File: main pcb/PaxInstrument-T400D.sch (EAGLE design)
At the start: 88 parts, among them IC2 NC7S00DBV, J1 MICRO-SDCARD-CONNECTOR-330006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, Q1 DMP2035U-7, U2 APX809, U3 MCP73831, U4 MIC5219-3.3V, X1 FH12-12S-1S, X2 FH12-12S-0.5SH, Y1 RESONATORSMD

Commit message: - Not sure what changed. This is still just playing around.
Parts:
- removed ICSP, ICSP1: ICSP, PaxInstrument-T400:SPARKFUN-CONNECTORS_M03X2PAX
- added JP13, JP14, JP15, JP16, JP17: M01PTH, SparkFun-Connectors:M01PTH
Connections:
- net 3.3V: no longer ICSP1.6
- net DATA1: no longer ICSP1.3
- net DATA2: no longer ICSP1.4
- net GND: no longer ICSP.6, ICSP1.5
- net MISO: now also JP13.1; no longer ICSP.1
- net MOSI: now also JP17.1; no longer ICSP.4
- net RESET: now also JP15.1; no longer ICSP.5
- net SCK: now also JP14.1; no longer ICSP.3
- net SCL: no longer ICSP1.1
- net SDA: no longer ICSP1.2
- net VBUS_IN: now also JP16.1; no longer ICSP.2
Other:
- note removed: "ICSP"
- note removed: "Programming"

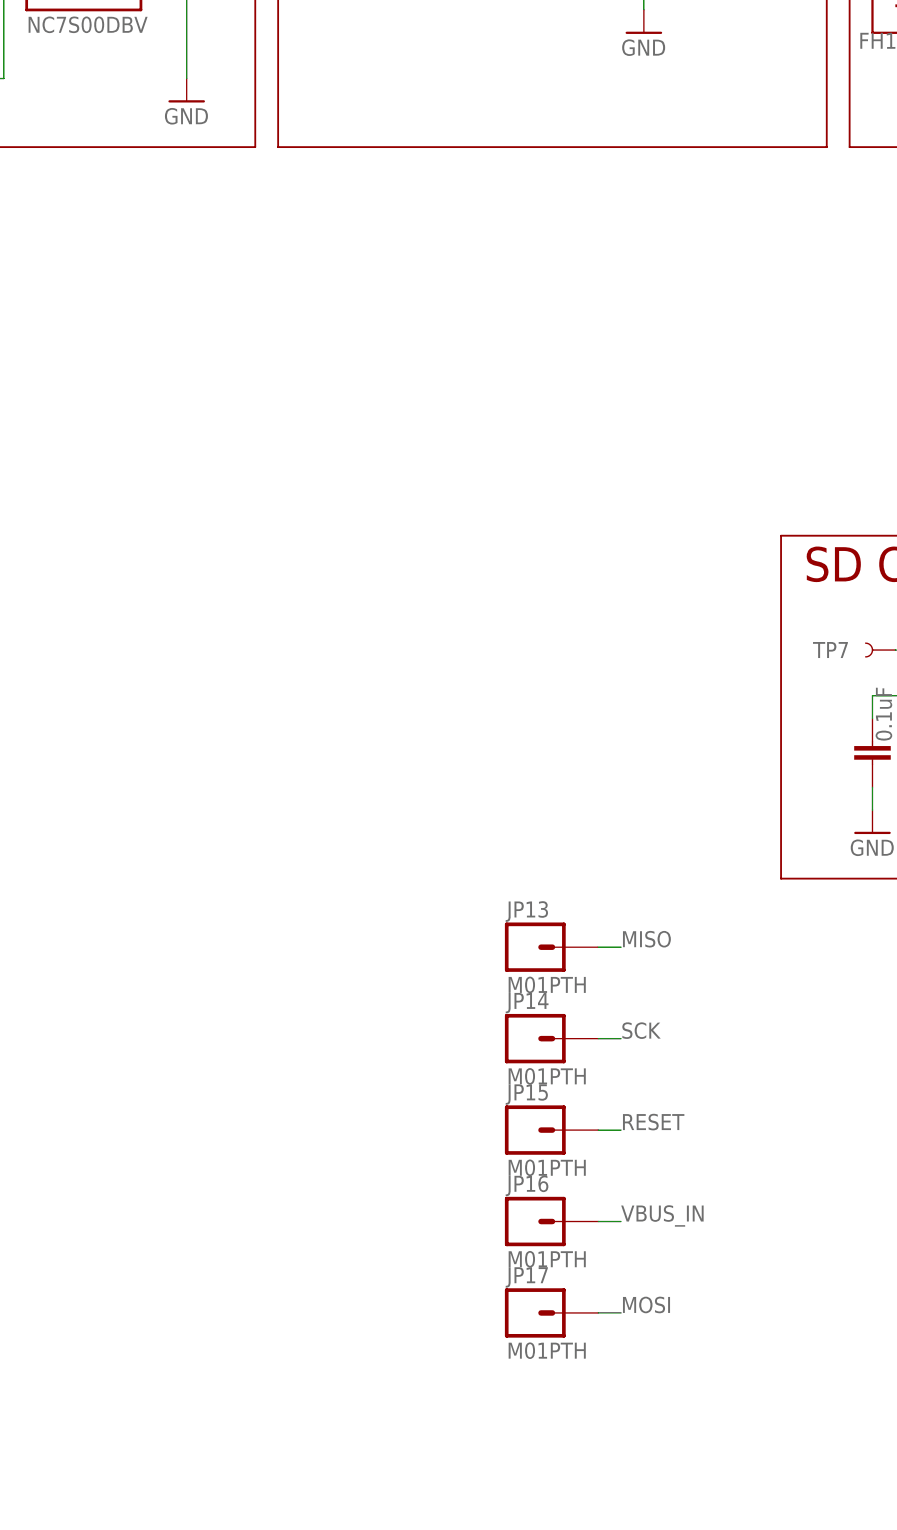
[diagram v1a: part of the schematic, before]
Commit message: Lengthened the modules.
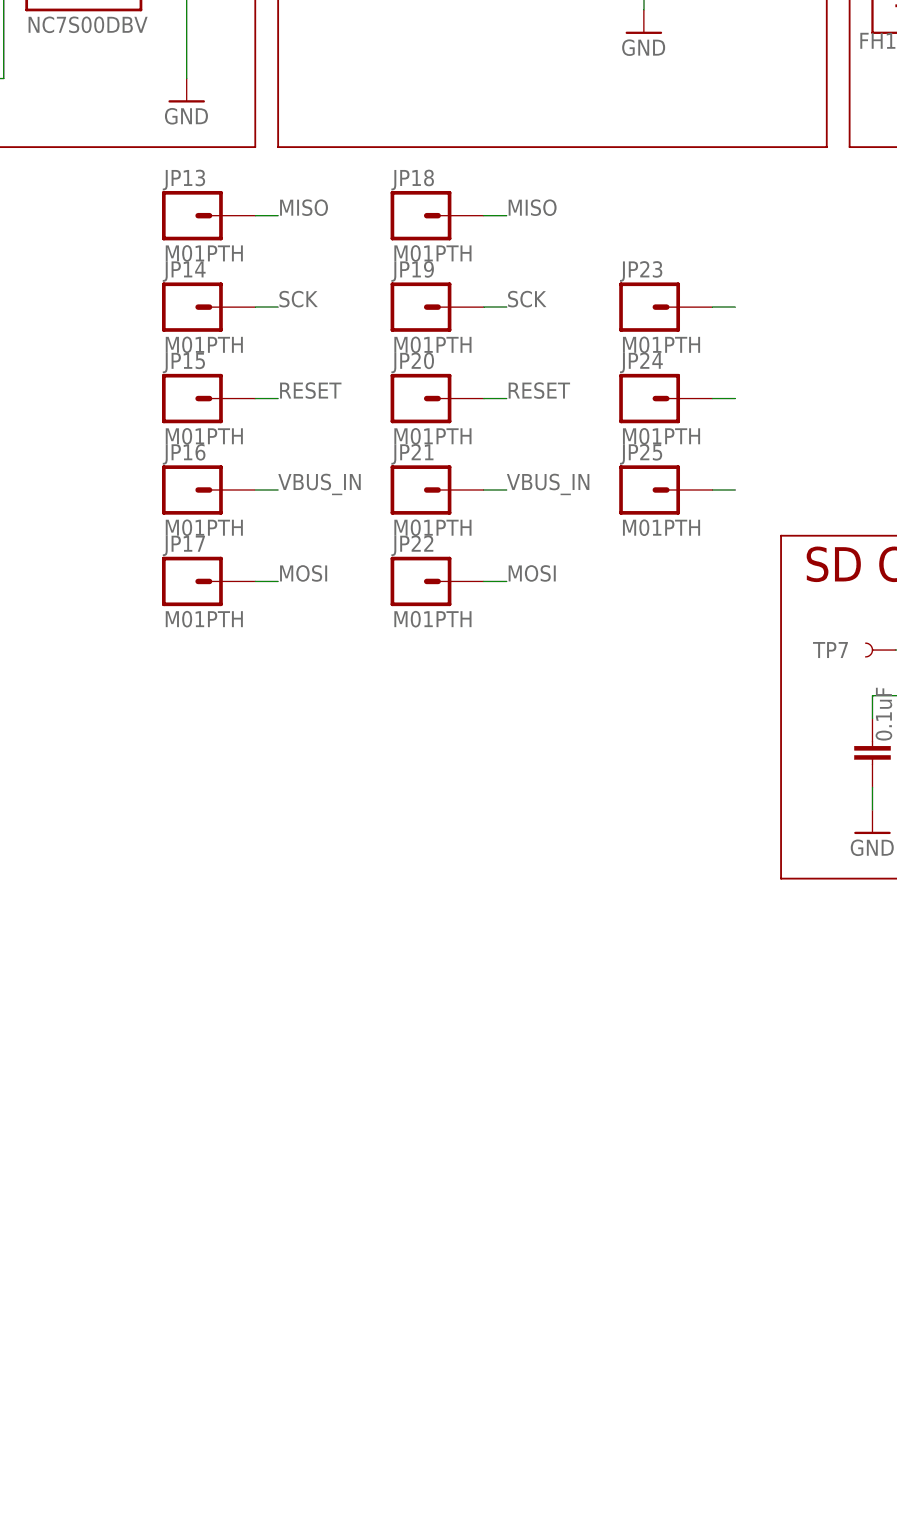
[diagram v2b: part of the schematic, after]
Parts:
- added JP18, JP19, JP20, JP21, JP22, JP23, JP24, JP25: M01PTH, SparkFun-Connectors:M01PTH
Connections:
- new net MOSI2: JP25.1
- new net RESET1: JP23.1
- new net VBUS_IN1: JP24.1
- net MISO: now also JP18.1
- net MOSI: now also JP22.1
- net RESET: now also JP20.1
- net SCK: now also JP19.1
- net VBUS_IN: now also JP21.1
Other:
- moved on the sheet: JP13, JP14, JP15, JP16, JP17
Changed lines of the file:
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@@
 <part name="JP16" library="SparkFun-Connectors" deviceset="M01" device="PTH"/>
 <part name="JP17" library="SparkFun-Connectors" deviceset="M01" device="PTH"/>
+<part name="JP18" library="SparkFun-Connectors" deviceset="M01" device="PTH"/>
+<part name="JP19" library="SparkFun-Connectors" deviceset="M01" device="PTH"/>
+<part name="JP20" library="SparkFun-Connectors" deviceset="M01" device="PTH"/>
+<part name="JP21" library="SparkFun-Connectors" deviceset="M01" device="PTH"/>
+<part name="JP22" library="SparkFun-Connectors" deviceset="M01" device="PTH"/>
+<part name="JP23" library="SparkFun-Connectors" deviceset="M01" device="PTH"/>
+<part name="JP24" library="SparkFun-Connectors" deviceset="M01" device="PTH"/>
+<part name="JP25" library="SparkFun-Connectors" deviceset="M01" device="PTH"/>
 </parts>
 <sheets>
@@
 <instance part="JP11" gate="G$1" x="172.72" y="157.48"/>
 <instance part="JP12" gate="G$1" x="172.72" y="147.32"/>
-<instance part="JP13" gate="G$1" x="251.46" y="106.68"/>
-<instance part="JP14" gate="G$1" x="251.46" y="96.52"/>
-<instance part="JP15" gate="G$1" x="251.46" y="86.36"/>
-<instance part="JP16" gate="G$1" x="251.46" y="76.2"/>
-<instance part="JP17" gate="G$1" x="251.46" y="66.04"/>
+<instance part="JP13" gate="G$1" x="213.36" y="187.96"/>
+<instance part="JP14" gate="G$1" x="213.36" y="177.8"/>
+<instance part="JP15" gate="G$1" x="213.36" y="167.64"/>
+<instance part="JP16" gate="G$1" x="213.36" y="157.48"/>
+<instance part="JP17" gate="G$1" x="213.36" y="147.32"/>
+<instance part="JP18" gate="G$1" x="238.76" y="187.96"/>
+<instance part="JP19" gate="G$1" x="238.76" y="177.8"/>
+<instance part="JP20" gate="G$1" x="238.76" y="167.64"/>
+<instance part="JP21" gate="G$1" x="238.76" y="157.48"/>
+<instance part="JP22" gate="G$1" x="238.76" y="147.32"/>
+<instance part="JP23" gate="G$1" x="264.16" y="177.8"/>
+<instance part="JP24" gate="G$1" x="264.16" y="167.64"/>
+<instance part="JP25" gate="G$1" x="264.16" y="157.48"/>
 </instances>
 <busses>
@@
 <segment>
 <pinref part="JP15" gate="G$1" pin="1"/>
-<wire x1="259.08" y1="86.36" x2="261.62" y2="86.36" width="0.1524" layer="91"/>
-<label x="261.62" y="86.36" size="1.778" layer="95"/>
+<wire x1="220.98" y1="167.64" x2="223.52" y2="167.64" width="0.1524" layer="91"/>
+<label x="223.52" y="167.64" size="1.778" layer="95"/>
+</segment>
+<segment>
+<pinref part="JP20" gate="G$1" pin="1"/>
+<wire x1="246.38" y1="167.64" x2="248.92" y2="167.64" width="0.1524" layer="91"/>
+<label x="248.92" y="167.64" size="1.778" layer="95"/>
 </segment>
 </net>
@@
 <segment>
 <pinref part="JP13" gate="G$1" pin="1"/>
-<wire x1="259.08" y1="106.68" x2="261.62" y2="106.68" width="0.1524" layer="91"/>
-<label x="261.62" y="106.68" size="1.778" layer="95"/>
+<wire x1="220.98" y1="187.96" x2="223.52" y2="187.96" width="0.1524" layer="91"/>
+<label x="223.52" y="187.96" size="1.778" layer="95"/>
+</segment>
+<segment>
+<pinref part="JP18" gate="G$1" pin="1"/>
+<wire x1="246.38" y1="187.96" x2="248.92" y2="187.96" width="0.1524" layer="91"/>
+<label x="248.92" y="187.96" size="1.778" layer="95"/>
 </segment>
 </net>
@@
 <segment>
 <pinref part="JP17" gate="G$1" pin="1"/>
-<wire x1="259.08" y1="66.04" x2="261.62" y2="66.04" width="0.1524" layer="91"/>
-<label x="261.62" y="66.04" size="1.778" layer="95"/>
+<wire x1="220.98" y1="147.32" x2="223.52" y2="147.32" width="0.1524" layer="91"/>
+<label x="223.52" y="147.32" size="1.778" layer="95"/>
+</segment>
+<segment>
+<pinref part="JP22" gate="G$1" pin="1"/>
+<wire x1="246.38" y1="147.32" x2="248.92" y2="147.32" width="0.1524" layer="91"/>
+<label x="248.92" y="147.32" size="1.778" layer="95"/>
 </segment>
 </net>
@@
 <segment>
 <pinref part="JP14" gate="G$1" pin="1"/>
-<wire x1="259.08" y1="96.52" x2="261.62" y2="96.52" width="0.1524" layer="91"/>
-<label x="261.62" y="96.52" size="1.778" layer="95"/>
+<wire x1="220.98" y1="177.8" x2="223.52" y2="177.8" width="0.1524" layer="91"/>
+<label x="223.52" y="177.8" size="1.778" layer="95"/>
+</segment>
+<segment>
+<pinref part="JP19" gate="G$1" pin="1"/>
+<wire x1="246.38" y1="177.8" x2="248.92" y2="177.8" width="0.1524" layer="91"/>
+<label x="248.92" y="177.8" size="1.778" layer="95"/>
 </segment>
 </net>
@@
 <segment>
 <pinref part="JP16" gate="G$1" pin="1"/>
-<wire x1="259.08" y1="76.2" x2="261.62" y2="76.2" width="0.1524" layer="91"/>
-<label x="261.62" y="76.2" size="1.778" layer="95"/>
+<wire x1="220.98" y1="157.48" x2="223.52" y2="157.48" width="0.1524" layer="91"/>
+<label x="223.52" y="157.48" size="1.778" layer="95"/>
+</segment>
+<segment>
+<pinref part="JP21" gate="G$1" pin="1"/>
+<wire x1="246.38" y1="157.48" x2="248.92" y2="157.48" width="0.1524" layer="91"/>
+<label x="248.92" y="157.48" size="1.778" layer="95"/>
 </segment>
 </net>
@@
 </segment>
 </net>
+<net name="RESET1" class="0">
+<segment>
+<pinref part="JP23" gate="G$1" pin="1"/>
+<wire x1="271.78" y1="177.8" x2="274.32" y2="177.8" width="0.1524" layer="91"/>
+</segment>
+</net>
+<net name="MOSI2" class="0">
+<segment>
+<pinref part="JP25" gate="G$1" pin="1"/>
+<wire x1="271.78" y1="157.48" x2="274.32" y2="157.48" width="0.1524" layer="91"/>
+</segment>
+</net>
+<net name="VBUS_IN1" class="1">
+<segment>
+<pinref part="JP24" gate="G$1" pin="1"/>
+<wire x1="271.78" y1="167.64" x2="274.32" y2="167.64" width="0.1524" layer="91"/>
+</segment>
+</net>
